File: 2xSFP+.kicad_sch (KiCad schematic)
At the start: 55 parts, among them J2 SFP+_Bel_SS-79100-010, U5 PCA9539AHF

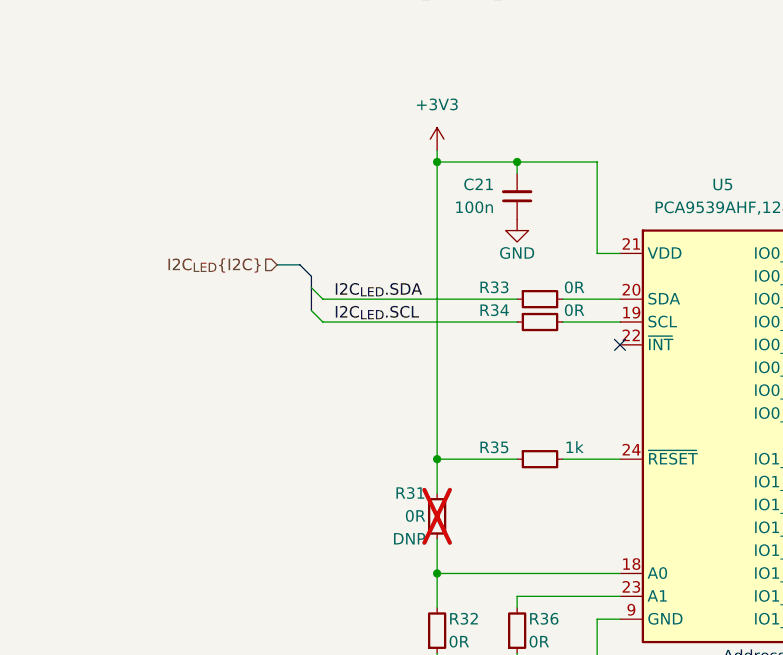
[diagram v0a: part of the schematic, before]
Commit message: [#58137] Add power sequencing and reset
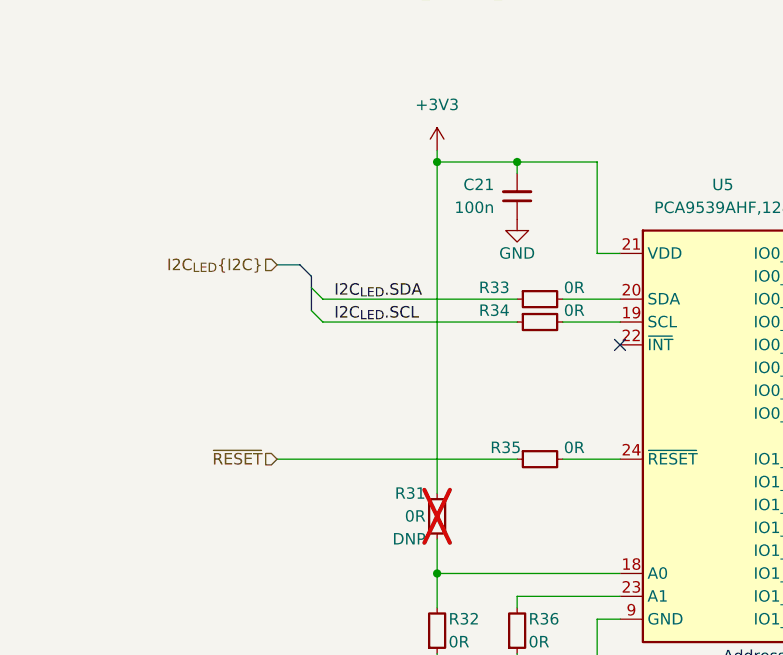
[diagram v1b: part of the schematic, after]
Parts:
- removed R35: R_1k_0402, antmicro-footprints:R_0402_1005Metric, symbol antmicroResistors0402:R_1k_0402
- added R35: R_0R_0402, antmicro-footprints:R_0402_1005Metric, symbol antmicroResistors0402:R_0R_0402
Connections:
- net at U5.24 (~{RESET}): now also R35.2
- new net ~{RESET}: R35.1
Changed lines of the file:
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@@
   (junction (at 250.19 35.56) (diameter 0) (color 0 0 0 0)
   )
-  (junction (at 160.02 251.46) (diameter 0) (color 0 0 0 0)
-  )
   (junction (at 241.3 35.56) (diameter 0) (color 0 0 0 0)
   )
@@
     (stroke (width 0) (type default))
   )
-  (wire (pts (xy 160.02 251.46) (xy 160.02 218.44))
+  (wire (pts (xy 160.02 218.44) (xy 160.02 255.27))
     (stroke (width 0) (type default))
   )
@@
     (stroke (width 0) (type default))
   )
-  (wire (pts (xy 160.02 251.46) (xy 168.91 251.46))
-    (stroke (width 0) (type default))
-  )
   (wire (pts (xy 168.91 266.7) (xy 180.34 266.7))
     (stroke (width 0) (type default))
@@
     (stroke (width 0) (type default))
   )
-  (wire (pts (xy 173.99 251.46) (xy 180.34 251.46))
-    (stroke (width 0) (type default))
-  )
   (wire (pts (xy 250.19 120.65) (xy 250.19 119.38))
     (stroke (width 0) (type default))
@@
     (stroke (width 0) (type default))
   )
+  (wire (pts (xy 173.99 251.46) (xy 180.34 251.46))
+    (stroke (width 0) (type default))
+  )
   (wire (pts (xy 299.72 113.03) (xy 303.53 113.03))
     (stroke (width 0) (type default))
@@
     (stroke (width 0) (type default))
   )
+  (wire (pts (xy 142.24 251.46) (xy 168.91 251.46))
+    (stroke (width 0) (type default))
+  )
   (wire (pts (xy 233.68 165.1) (xy 234.95 165.1))
     (stroke (width 0) (type default))
@@
     (stroke (width 0) (type default))
   )
-  (wire (pts (xy 160.02 255.27) (xy 160.02 251.46))
-    (stroke (width 0) (type default))
-  )
   (bus (pts (xy 142.24 66.04) (xy 175.26 66.04))
     (stroke (width 0) (type default))
@@
     (effects (font (size 1.27 1.27)) (justify right))
   )
+  (hierarchical_label "~{RESET}" (shape input) (at 142.24 251.46 180) (fields_autoplaced)
+    (effects (font (size 1.27 1.27)) (justify right))
+  )
   (hierarchical_label "10GKR_SFP1{10GBaseKR}" (shape input) (at 142.24 172.72 180) (fields_autoplaced)
     (effects (font (size 1.27 1.27)) (justify right))
@@
     )
   )
-  (symbol (lib_id "antmicroResistors0402:R_1k_0402") (at 168.91 251.46 0) (unit 1)
-    (in_bom yes) (on_board yes) (dnp no)
-    (property "Reference" "R35" (at 166.37 250.19 0)
-      (effects (font (size 1.27 1.27) (thickness 0.15)))
-    )
-    (property "Value" "R_1k_0402" (at 189.23 264.16 0)
-      (effects (font (size 1.27 1.27) (thickness 0.15)) (justify left bottom) hide)
-    )
-    (property "Footprint" "antmicro-footprints:R_0402_1005Metric" (at 189.23 266.7 0)
-      (effects (font (size 1.27 1.27) (thickness 0.15)) (justify left bottom) hide)
-    )
-    (property "Datasheet" "https://www.bourns.com/docs/product-datasheets/cr.pdf" (at 189.23 269.24 0)
-      (effects (font (size 1.27 1.27) (thickness 0.15)) (justify left bottom) hide)
-    )
-    (property "MPN" "CR0402-FX-1001GLF" (at 189.23 271.78 0)
-      (effects (font (size 1.27 1.27) (thickness 0.15)) (justify left bottom) hide)
-    )
-    (property "Manufacturer" "Bourns" (at 189.23 274.32 0)
-      (effects (font (size 1.27 1.27) (thickness 0.15)) (justify left bottom) hide)
-    )
-    (property "License" "Apache-2.0" (at 189.23 276.86 0)
-      (effects (font (size 1.27 1.27) (thickness 0.15)) (justify left bottom) hide)
-    )
-    (property "Author" "Antmicro" (at 189.23 279.4 0)
-      (effects (font (size 1.27 1.27) (thickness 0.15)) (justify left bottom) hide)
-    )
-    (property "Val" "1k" (at 175.26 250.19 0)
-      (effects (font (size 1.27 1.27) (thickness 0.15)))
-    )
-    (property "Tolerance" "1%" (at 189.23 261.62 0)
-      (effects (font (size 1.27 1.27)) (justify left bottom) hide)
-    )
-    (pin "2")
-    (pin "1")
-    (instances
-      (project "com-express-7-baseboard"
-        (path "/1b8c34da-dad5-4b0b-8c4b-45db766c4dfa/bc90cc14-34f1-4905-9b90-ab809e861ec6"
-          (reference "R35") (unit 1)
-        )
-      )
-    )
-  )
   (symbol (lib_id "antmicropower:GND") (at 250.19 41.91 0) (mirror y) (unit 1)
     (in_bom yes) (on_board yes) (dnp no)
@@
         )
       )
+    )
+  )
+  (symbol (lib_id "antmicroResistors0402:R_0R_0402") (at 168.91 251.46 0) (unit 1)
+    (in_bom yes) (on_board yes) (dnp no)
+    (property "Reference" "R35" (at 167.64 250.19 0)
+      (effects (font (size 1.27 1.27) (thickness 0.15)))
+    )
+    (property "Value" "R_0R_0402" (at 189.23 264.16 0)
+      (effects (font (size 1.27 1.27) (thickness 0.15)) (justify left bottom) hide)
+    )
+    (property "Footprint" "antmicro-footprints:R_0402_1005Metric" (at 189.23 266.7 0)
+      (effects (font (size 1.27 1.27) (thickness 0.15)) (justify left bottom) hide)
+    )
+    (property "Datasheet" "https://industrial.panasonic.com/cdbs/www-data/pdf/RDA0000/AOA0000C301.pdf" (at 189.23 269.24 0)
+      (effects (font (size 1.27 1.27) (thickness 0.15)) (justify left bottom) hide)
+    )
+    (property "MPN" "ERJ2GE0R00X" (at 189.23 271.78 0)
+      (effects (font (size 1.27 1.27) (thickness 0.15)) (justify left bottom) hide)
+    )
+    (property "Manufacturer" "Panasonic" (at 189.23 274.32 0)
+      (effects (font (size 1.27 1.27) (thickness 0.15)) (justify left bottom) hide)
+    )
+    (property "License" "Apache-2.0" (at 189.23 276.86 0)
+      (effects (font (size 1.27 1.27) (thickness 0.15)) (justify left bottom) hide)
+    )
+    (property "Author" "Antmicro" (at 189.23 279.4 0)
+      (effects (font (size 1.27 1.27) (thickness 0.15)) (justify left bottom) hide)
+    )
+    (property "Val" "0R" (at 175.26 250.19 0)
+      (effects (font (size 1.27 1.27) (thickness 0.15)))
+    )
+    (property "Tolerance" "~" (at 189.23 261.62 0)
+      (effects (font (size 1.27 1.27)) (justify left bottom) hide)
+    )
+    (property "Current" "1A" (at 189.23 281.94 0)
+      (effects (font (size 1.27 1.27) (thickness 0.15)) (justify left bottom) hide)
+    )
+    (pin "1")
+    (pin "2")
+    (instances
+      (project "com-express-7-baseboard"
+        (path "/1b8c34da-dad5-4b0b-8c4b-45db766c4dfa/bc90cc14-34f1-4905-9b90-ab809e861ec6"
+          (reference "R35") (unit 1)
+        )
+      )

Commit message: Optimize BOM, reannotate
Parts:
- removed D7, D8: LED_G_0603_LTST-C190KGKT, antmicro-footprints:LED_0603_1608Metric_G, symbol antmicroLEDIndicationDiscrete:LED_G_0603_LTST-C190KGKT
- added D7, D8: LED_G_0603_LTST-C190GKT, antmicro-footprints:LED_0603_1608Metric_G, symbol antmicroLEDIndicationDiscrete:LED_G_0603_LTST-C190GKT
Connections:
- net SFP0_LEDG: now also D8.2
- net SFP1_LEDG: now also D7.2
- net at R65.1: now also D8.1
- net at R64.1: now also D7.1
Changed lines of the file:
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@@
-    )
-  )
-  (symbol (lib_id "antmicroLEDIndicationDiscrete:LED_G_0603_LTST-C190KGKT") (at 344.17 77.47 270) (unit 1)
-    (in_bom yes) (on_board yes) (dnp no) (fields_autoplaced)
-    (property "Reference" "D8" (at 347.98 80.01 90)
-      (effects (font (size 1.27 1.27) (thickness 0.15)) (justify left))
-    )
-    (property "Value" "LED_G_0603_LTST-C190KGKT" (at 347.98 82.55 90)
-      (effects (font (size 1.27 1.27) (thickness 0.15)) (justify left) hide)
-    )
-    (property "Footprint" "antmicro-footprints:LED_0603_1608Metric_G" (at 334.01 100.33 0)
-      (effects (font (size 1.27 1.27) (thickness 0.15)) (justify left bottom) hide)
-    )
-    (property "Datasheet" "https://media.digikey.com/pdf/Data%20Sheets/Lite-On%20PDFs/LTST-C190KGKT.pdf" (at 331.47 100.33 0)
-      (effects (font (size 1.27 1.27) (thickness 0.15)) (justify left bottom) hide)
-    )
-    (property "MPN" "LTST-C190KGKT" (at 347.98 82.55 90)
-      (effects (font (size 1.27 1.27) (thickness 0.15)) (justify left))
-    )
-    (property "Manufacturer" "Lite-On" (at 326.39 100.33 0)
-      (effects (font (size 1.27 1.27) (thickness 0.15)) (justify left bottom) hide)
-    )
-    (property "Author" "Antmicro" (at 323.85 100.33 0)
-      (effects (font (size 1.27 1.27) (thickness 0.15)) (justify left bottom) hide)
-    )
-    (property "License" "Apache-2.0" (at 321.31 100.33 0)
-      (effects (font (size 1.27 1.27) (thickness 0.15)) (justify left bottom) hide)
-    )
-    (property "VSD_class" "LED" (at 318.77 100.33 0)
-      (effects (font (size 1.27 1.27)) (justify left bottom) hide)
-    )
-    (pin "1")
-    (pin "2")
-    (instances
-      (project "com-express-7-baseboard"
-        (path "/1b8c34da-dad5-4b0b-8c4b-45db766c4dfa/bc90cc14-34f1-4905-9b90-ab809e861ec6"
-          (reference "D8") (unit 1)
-        )
-      )
     )
   )
@@
     )
   )
+  (symbol (lib_id "antmicroLEDIndicationDiscrete:LED_G_0603_LTST-C190GKT") (at 344.17 77.47 270) (unit 1)
+    (in_bom yes) (on_board yes) (dnp no)
+    (property "Reference" "D8" (at 347.98 80.0099 90)
+      (effects (font (size 1.27 1.27)) (justify left))
+    )
+    (property "Value" "LED_G_0603_LTST-C190GKT" (at 336.55 100.33 0)
+      (effects (font (size 1.27 1.27) (thickness 0.15)) (justify left bottom) hide)
+    )
+    (property "Footprint" "antmicro-footprints:LED_0603_1608Metric_G" (at 334.01 100.33 0)
+      (effects (font (size 1.27 1.27) (thickness 0.15)) (justify left bottom) hide)
+    )
+    (property "Datasheet" "https://media.digikey.com/pdf/Data%20Sheets/Lite-On%20PDFs/LTST-C190GKT.pdf" (at 331.47 100.33 0)
+      (effects (font (size 1.27 1.27) (thickness 0.15)) (justify left bottom) hide)
+    )
+    (property "MPN" "LTST-C190GKT" (at 347.98 82.5499 90)
+      (effects (font (size 1.27 1.27) (thickness 0.15)) (justify left))
+    )
+    (property "Manufacturer" "Lite-On Inc." (at 326.39 100.33 0)
+      (effects (font (size 1.27 1.27) (thickness 0.15)) (justify left bottom) hide)
+    )
+    (property "Author" "Antmicro" (at 323.85 100.33 0)
+      (effects (font (size 1.27 1.27) (thickness 0.15)) (justify left bottom) hide)
+    )
+    (property "License" "Apache-2.0" (at 321.31 100.33 0)
+      (effects (font (size 1.27 1.27) (thickness 0.15)) (justify left bottom) hide)
+    )
+    (pin "1")
+    (pin "2")
+    (instances
+      (project "com-express-7-baseboard"
+        (path "/1b8c34da-dad5-4b0b-8c4b-45db766c4dfa/bc90cc14-34f1-4905-9b90-ab809e861ec6"
+          (reference "D8") (unit 1)
+        )
+      )
+    )
+  )
   (symbol (lib_id "antmicroTestPoints:TP_0.75mm_SMD") (at 233.68 165.1 180) (unit 1)
     (in_bom no) (on_board yes) (dnp no)
@@
         (path "/1b8c34da-dad5-4b0b-8c4b-45db766c4dfa/bc90cc14-34f1-4905-9b90-ab809e861ec6"
           (reference "R54") (unit 1)
+        )
+      )
+    )
+  )
+  (symbol (lib_id "antmicroLEDIndicationDiscrete:LED_G_0603_LTST-C190GKT") (at 342.9 154.94 270) (unit 1)
+    (in_bom yes) (on_board yes) (dnp no)
+    (property "Reference" "D7" (at 346.71 157.4799 90)
+      (effects (font (size 1.27 1.27)) (justify left))
+    )
+    (property "Value" "LED_G_0603_LTST-C190GKT" (at 335.28 177.8 0)
+      (effects (font (size 1.27 1.27) (thickness 0.15)) (justify left bottom) hide)
+    )
+    (property "Footprint" "antmicro-footprints:LED_0603_1608Metric_G" (at 332.74 177.8 0)
+      (effects (font (size 1.27 1.27) (thickness 0.15)) (justify left bottom) hide)
+    )
+    (property "Datasheet" "https://media.digikey.com/pdf/Data%20Sheets/Lite-On%20PDFs/LTST-C190GKT.pdf" (at 330.2 177.8 0)
+      (effects (font (size 1.27 1.27) (thickness 0.15)) (justify left bottom) hide)
+    )
+    (property "MPN" "LTST-C190GKT" (at 346.71 160.0199 90)
+      (effects (font (size 1.27 1.27) (thickness 0.15)) (justify left))
+    )
+    (property "Manufacturer" "Lite-On Inc." (at 325.12 177.8 0)
+      (effects (font (size 1.27 1.27) (thickness 0.15)) (justify left bottom) hide)
+    )
+    (property "Author" "Antmicro" (at 322.58 177.8 0)
+      (effects (font (size 1.27 1.27) (thickness 0.15)) (justify left bottom) hide)
+    )
+    (property "License" "Apache-2.0" (at 320.04 177.8 0)
+      (effects (font (size 1.27 1.27) (thickness 0.15)) (justify left bottom) hide)
+    )
+    (pin "1")
+    (pin "2")
+    (instances
+      (project "com-express-7-baseboard"
+        (path "/1b8c34da-dad5-4b0b-8c4b-45db766c4dfa/bc90cc14-34f1-4905-9b90-ab809e861ec6"
+          (reference "D7") (unit 1)
         )
       )
@@
         )
       )
-    )
-  )
-  (symbol (lib_id "antmicroLEDIndicationDiscrete:LED_G_0603_LTST-C190KGKT") (at 342.9 154.94 270) (unit 1)
-    (in_bom yes) (on_board yes) (dnp no) (fields_autoplaced)
-    (property "Reference" "D7" (at 346.71 157.48 90)
-      (effects (font (size 1.27 1.27) (thickness 0.15)) (justify left))
-    )
-    (property "Value" "LED_G_0603_LTST-C190KGKT" (at 346.71 160.02 90)
-      (effects (font (size 1.27 1.27) (thickness 0.15)) (justify left) hide)
-    )
-    (property "Footprint" "antmicro-footprints:LED_0603_1608Metric_G" (at 332.74 177.8 0)
-      (effects (font (size 1.27 1.27) (thickness 0.15)) (justify left bottom) hide)
-    )
-    (property "Datasheet" "https://media.digikey.com/pdf/Data%20Sheets/Lite-On%20PDFs/LTST-C190KGKT.pdf" (at 330.2 177.8 0)
-      (effects (font (size 1.27 1.27) (thickness 0.15)) (justify left bottom) hide)
-    )
-    (property "MPN" "LTST-C190KGKT" (at 346.71 160.02 90)
-      (effects (font (size 1.27 1.27) (thickness 0.15)) (justify left))
-    )
-    (property "Manufacturer" "Lite-On" (at 325.12 177.8 0)
-      (effects (font (size 1.27 1.27) (thickness 0.15)) (justify left bottom) hide)
-    )
-    (property "Author" "Antmicro" (at 322.58 177.8 0)
-      (effects (font (size 1.27 1.27) (thickness 0.15)) (justify left bottom) hide)
-    )
-    (property "License" "Apache-2.0" (at 320.04 177.8 0)
-      (effects (font (size 1.27 1.27) (thickness 0.15)) (justify left bottom) hide)
-    )
-    (property "VSD_class" "LED" (at 317.5 177.8 0)
-      (effects (font (size 1.27 1.27)) (justify left bottom) hide)
-    )
-    (pin "1")
-    (pin "2")
-    (instances
-      (project "com-express-7-baseboard"
-        (path "/1b8c34da-dad5-4b0b-8c4b-45db766c4dfa/bc90cc14-34f1-4905-9b90-ab809e861ec6"
-          (reference "D7") (unit 1)
-        )
-      )

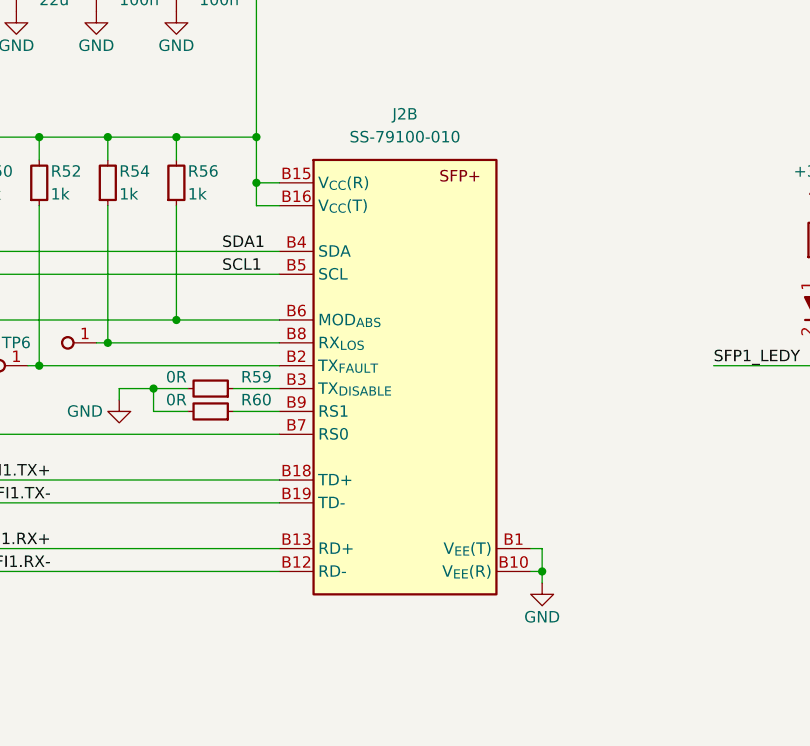
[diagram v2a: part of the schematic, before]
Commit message: [#58904] Fix DRC
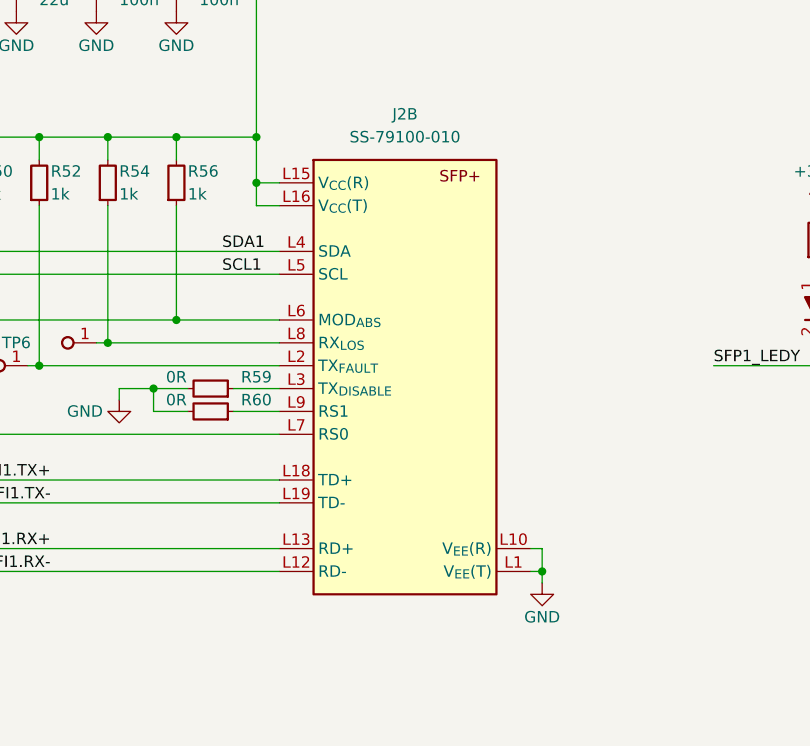
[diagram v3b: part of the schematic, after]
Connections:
- net +3V3: now also J2.L15 (V_{CC}(R)), J2.L16 (V_{CC}(T)); no longer J2.B15 (V_{CC}(R)), J2.B16 (V_{CC}(T))
- net GND: now also J2.L1 (V_{EE}(T)), J2.L10 (V_{EE}(R)), J2.L11 (V_{EE}(R)), J2.L14 (V_{EE}(R)), J2.L17 (V_{EE}(T)), J2.L20 (V_{EE}(T)); no longer J2.B1 (V_{EE}(T)), J2.B10 (V_{EE}(R)), J2.B11 (V_{EE}(R)), J2.B14 (V_{EE}(R)), J2.B17 (V_{EE}(T)), J2.B20 (V_{EE}(T))
- net SCL1: now also J2.L5 (SCL); no longer J2.B5 (SCL)
- net SDA1: now also J2.L4 (SDA); no longer J2.B4 (SDA)
- net SFI1.RX+: now also J2.L13 (RD+); no longer J2.B13 (RD+)
- net SFI1.RX-: now also J2.L12 (RD-); no longer J2.B12 (RD-)
- net SFI1.TX+: now also J2.L18 (TD+); no longer J2.B18 (TD+)
- net SFI1.TX-: now also J2.L19 (TD-); no longer J2.B19 (TD-)
- net at R42.2, R56.1: now also J2.L6 (MOD_{ABS}); no longer J2.B6 (MOD_{ABS})
- net at R52.1, TP4.1: now also J2.L2 (TX_{FAULT}); no longer J2.B2 (TX_{FAULT})
- net at R59.1: now also J2.L3 (TX_{DISABLE}); no longer J2.B3 (TX_{DISABLE})
- net at R50.1: now also J2.L7 (RS0); no longer J2.B7 (RS0)
- net at R54.1, TP6.1: now also J2.L8 (RX_{LOS}); no longer J2.B8 (RX_{LOS})
- net at R60.1: now also J2.L9 (RS1); no longer J2.B9 (RS1)
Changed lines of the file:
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@@
       (effects (font (size 1.27 1.27) (thickness 0.15)) (justify left bottom) hide)
     )
-    (pin "B9")
+    (pin "L1")
     (pin "T9")
-    (pin "B6")
-    (pin "B16")
+    (pin "L10")
+    (pin "L11")
     (pin "T8")
-    (pin "B13")
+    (pin "L12")
     (pin "T6")
-    (pin "B18")
-    (pin "B4")
-    (pin "B19")
+    (pin "L13")
+    (pin "L14")
+    (pin "L15")
     (pin "T14")
     (pin "T11")
@@
     (pin "T12")
     (pin "T3")
-    (pin "B17")
+    (pin "L16")
     (pin "T19")
     (pin "T20")
-    (pin "B3")
-    (pin "B10")
-    (pin "B11")
+    (pin "L17")
+    (pin "L18")
+    (pin "L19")
     (pin "T17")
     (pin "T7")
-    (pin "B5")
-    (pin "B8")
-    (pin "B15")
-    (pin "B7")
+    (pin "L2")
+    (pin "L20")
+    (pin "L3")
+    (pin "L4")
     (pin "T2")
     (pin "T13")
     (pin "T5")
     (pin "T18")
-    (pin "B14")
-    (pin "B2")
-    (pin "B20")
+    (pin "L5")
+    (pin "L6")
+    (pin "L7")
     (pin "T16")
     (pin "T4")
-    (pin "B1")
+    (pin "L8")
     (pin "T15")
-    (pin "B12")
+    (pin "L9")
     (pin "SH")
     (pin "T1")
@@
       (effects (font (size 1.27 1.27) (thickness 0.15)) (justify left bottom) hide)
     )
-    (pin "B9")
+    (pin "L14")
     (pin "T9")
-    (pin "B6")
-    (pin "B16")
+    (pin "L1")
+    (pin "L10")
     (pin "T8")
-    (pin "B13")
+    (pin "L12")
     (pin "T6")
-    (pin "B18")
-    (pin "B4")
-    (pin "B19")
+    (pin "L13")
+    (pin "L15")
+    (pin "L16")
     (pin "T14")
     (pin "T11")
@@
     (pin "T12")
     (pin "T3")
-    (pin "B17")
+    (pin "L11")
     (pin "T19")
     (pin "T20")
-    (pin "B3")
-    (pin "B10")
-    (pin "B11")
+    (pin "L17")
+    (pin "L18")
+    (pin "L19")
     (pin "T17")
     (pin "T7")
-    (pin "B5")
-    (pin "B8")
-    (pin "B15")
-    (pin "B7")
+    (pin "L2")
+    (pin "L20")
+    (pin "L3")
+    (pin "L4")
     (pin "T2")
     (pin "T13")
     (pin "T5")
     (pin "T18")
-    (pin "B14")
-    (pin "B2")
-    (pin "B20")
+    (pin "L5")
+    (pin "L6")
+    (pin "L7")
     (pin "T16")
     (pin "T4")
-    (pin "B1")
+    (pin "L8")
     (pin "T15")
-    (pin "B12")
+    (pin "L9")
     (pin "SH")
     (pin "T1")
